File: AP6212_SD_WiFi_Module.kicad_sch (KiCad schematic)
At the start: 21 parts, among them J1 Conn_Coaxial, J2 TF_Card, U1 AP6212, X1 32.768KHz, Y1 26MHz

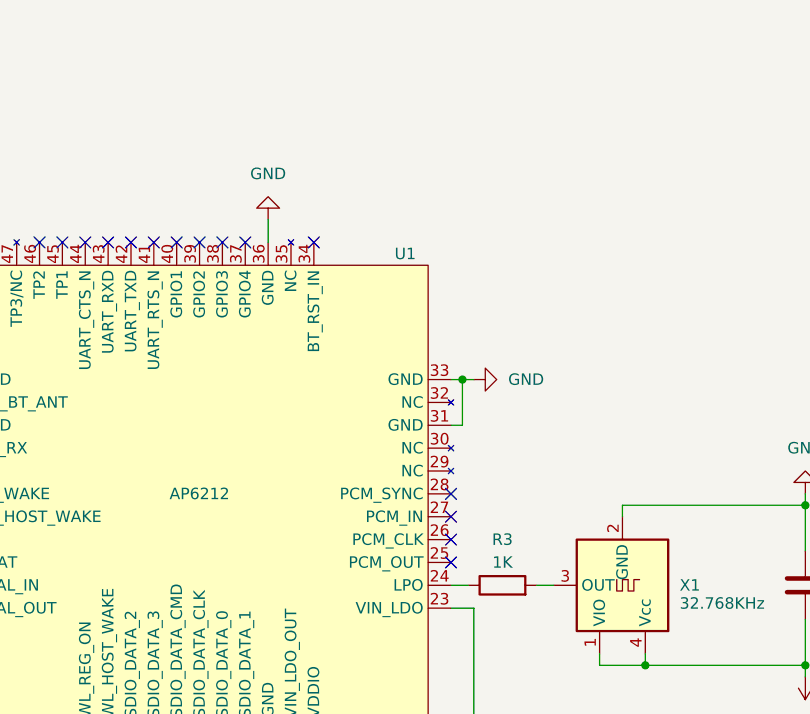
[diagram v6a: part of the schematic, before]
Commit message: BT_RST_N must be driven high or low(not left floating)
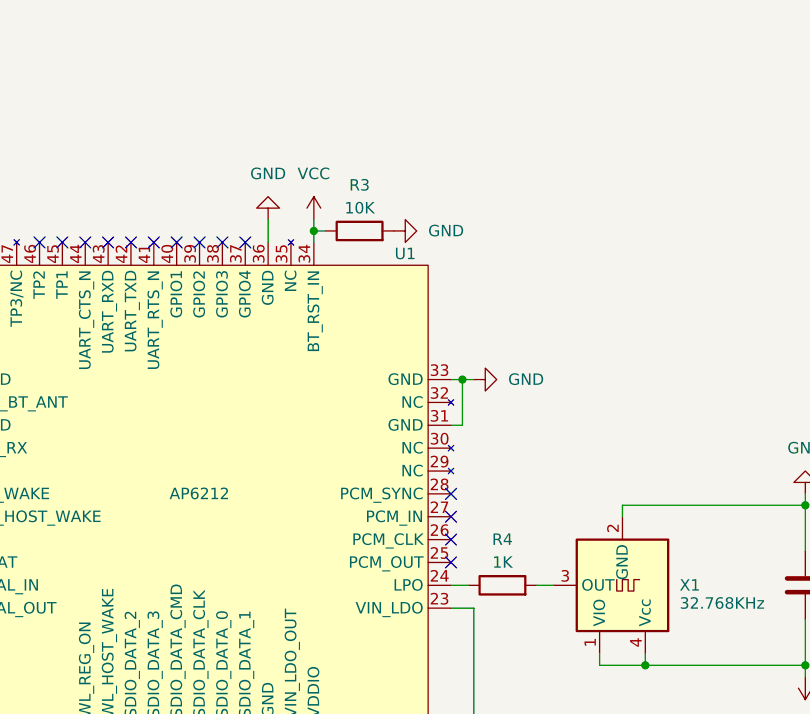
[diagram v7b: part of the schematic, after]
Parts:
- added R3: 10K, Resistor_SMD:R_0603_1608Metric, symbol Device:R
- renumbered R3 to R4
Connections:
- net GND: now also R3.2
- net VCC: now also U1.34 (BT_RST_IN), R3.1
- no-connect marks 19 -> 18
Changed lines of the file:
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@@
   (junction (at 222.25 156.21) (diameter 0) (color 0 0 0 0)
+  )
+  (junction (at 185.42 107.95) (diameter 0) (color 0 0 0 0)
   )
   (junction (at 110.49 147.32) (diameter 0) (color 0 0 0 0)
@@
   (no_connect (at 144.78 137.16))
   (no_connect (at 165.1 109.22))
-  (no_connect (at 185.42 109.22))
   (no_connect (at 200.66 144.78))
   (no_connect (at 170.18 109.22))
@@
     (stroke (width 0) (type default))
   )
+  (wire (pts (xy 185.42 107.95) (xy 185.42 109.22))
+    (stroke (width 0) (type default))
+  )
   (wire (pts (xy 120.65 97.79) (xy 120.65 110.49))
     (stroke (width 0) (type default))
@@
     (stroke (width 0) (type default))
   )
+  (wire (pts (xy 185.42 106.68) (xy 185.42 107.95))
+    (stroke (width 0) (type default))
+  )
   (wire (pts (xy 200.66 129.54) (xy 201.93 129.54))
     (stroke (width 0) (type default))
@@
   )
   (wire (pts (xy 180.34 106.68) (xy 180.34 109.22))
+    (stroke (width 0) (type default))
+  )
+  (wire (pts (xy 185.42 107.95) (xy 186.69 107.95))
     (stroke (width 0) (type default))
   )
@@
   (symbol (lib_id "power:GND") (at 203.2 124.46 90) (unit 1)
     (in_bom yes) (on_board yes) (dnp no) (fields_autoplaced)
-    (property "Reference" "#PWR016" (at 209.55 124.46 0)
+    (property "Reference" "#PWR018" (at 209.55 124.46 0)
       (effects (font (size 1.27 1.27)) hide)
     )
@@
       (project "AP6212_SD_WiFi_Module"
         (path "/b65838ac-496f-4a8d-9112-1df66a66b3df"
-          (reference "#PWR016") (unit 1)
+          (reference "#PWR018") (unit 1)
         )
       )
@@
   (symbol (lib_id "power:VCC") (at 240.03 157.48 180) (unit 1)
     (in_bom yes) (on_board yes) (dnp no) (fields_autoplaced)
-    (property "Reference" "#PWR020" (at 240.03 153.67 0)
+    (property "Reference" "#PWR022" (at 240.03 153.67 0)
       (effects (font (size 1.27 1.27)) hide)
     )
@@
       (project "AP6212_SD_WiFi_Module"
         (path "/b65838ac-496f-4a8d-9112-1df66a66b3df"
-          (reference "#PWR020") (unit 1)
+          (reference "#PWR022") (unit 1)
         )
       )
@@
     )
   )
+  (symbol (lib_id "power:GND") (at 194.31 107.95 90) (unit 1)
+    (in_bom yes) (on_board yes) (dnp no) (fields_autoplaced)
+    (property "Reference" "#PWR017" (at 200.66 107.95 0)
+      (effects (font (size 1.27 1.27)) hide)
+    )
+    (property "Value" "GND" (at 198.12 107.95 90)
+      (effects (font (size 1.27 1.27)) (justify right))
+    )
+    (property "Footprint" "" (at 194.31 107.95 0)
+      (effects (font (size 1.27 1.27)) hide)
+    )
+    (property "Datasheet" "" (at 194.31 107.95 0)
+      (effects (font (size 1.27 1.27)) hide)
+    )
+    (pin "1")
+    (instances
+      (project "AP6212_SD_WiFi_Module"
+        (path "/b65838ac-496f-4a8d-9112-1df66a66b3df"
+          (reference "#PWR017") (unit 1)
+        )
+      )
+    )
+  )
   (symbol (lib_id "Device:C_Small") (at 115.57 110.49 90) (unit 1)
     (in_bom yes) (on_board yes) (dnp no) (fields_autoplaced)
@@
     )
   )
+  (symbol (lib_id "power:VCC") (at 185.42 106.68 0) (unit 1)
+    (in_bom yes) (on_board yes) (dnp no) (fields_autoplaced)
+    (property "Reference" "#PWR014" (at 185.42 110.49 0)
+      (effects (font (size 1.27 1.27)) hide)
+    )
+    (property "Value" "VCC" (at 185.42 101.6 0)
+      (effects (font (size 1.27 1.27)))
+    )
+    (property "Footprint" "" (at 185.42 106.68 0)
+      (effects (font (size 1.27 1.27)) hide)
+    )
+    (property "Datasheet" "" (at 185.42 106.68 0)
+      (effects (font (size 1.27 1.27)) hide)
+    )
+    (pin "1")
+    (instances
+      (project "AP6212_SD_WiFi_Module"
+        (path "/b65838ac-496f-4a8d-9112-1df66a66b3df"
+          (reference "#PWR014") (unit 1)
+        )
+      )
+    )
+  )
   (symbol (lib_id "power:VCC") (at 262.89 134.62 90) (mirror x) (unit 1)
     (in_bom yes) (on_board yes) (dnp no) (fields_autoplaced)
-    (property "Reference" "#PWR022" (at 266.7 134.62 0)
+    (property "Reference" "#PWR024" (at 266.7 134.62 0)
       (effects (font (size 1.27 1.27)) hide)
     )
@@
       (project "AP6212_SD_WiFi_Module"
         (path "/b65838ac-496f-4a8d-9112-1df66a66b3df"
-          (reference "#PWR022") (unit 1)
+          (reference "#PWR024") (unit 1)
         )
       )
@@
   (symbol (lib_id "power:VCC") (at 186.69 166.37 270) (unit 1)
     (in_bom yes) (on_board yes) (dnp no) (fields_autoplaced)
-    (property "Reference" "#PWR015" (at 182.88 166.37 0)
+    (property "Reference" "#PWR016" (at 182.88 166.37 0)
       (effects (font (size 1.27 1.27)) hide)
     )
@@
       (project "AP6212_SD_WiFi_Module"
         (path "/b65838ac-496f-4a8d-9112-1df66a66b3df"
+          (reference "#PWR016") (unit 1)
+        )
+      )
+    )
+  )
+  (symbol (lib_id "power:GND") (at 185.42 177.8 0) (unit 1)
+    (in_bom yes) (on_board yes) (dnp no) (fields_autoplaced)
+    (property "Reference" "#PWR015" (at 185.42 184.15 0)
+      (effects (font (size 1.27 1.27)) hide)
+    )
+    (property "Value" "GND" (at 185.42 182.88 0)
+      (effects (font (size 1.27 1.27)))
+    )
+    (property "Footprint" "" (at 185.42 177.8 0)
+      (effects (font (size 1.27 1.27)) hide)
+    )
+    (property "Datasheet" "" (at 185.42 177.8 0)
+      (effects (font (size 1.27 1.27)) hide)
+    )
+    (pin "1")
+    (instances
+      (project "AP6212_SD_WiFi_Module"
+        (path "/b65838ac-496f-4a8d-9112-1df66a66b3df"
           (reference "#PWR015") (unit 1)
-        )
-      )
-    )
-  )
-  (symbol (lib_id "power:GND") (at 185.42 177.8 0) (unit 1)
-    (in_bom yes) (on_board yes) (dnp no) (fields_autoplaced)
-    (property "Reference" "#PWR014" (at 185.42 184.15 0)
-      (effects (font (size 1.27 1.27)) hide)
-    )
-    (property "Value" "GND" (at 185.42 182.88 0)
-      (effects (font (size 1.27 1.27)))
-    )
-    (property "Footprint" "" (at 185.42 177.8 0)
-      (effects (font (size 1.27 1.27)) hide)
-    )
-    (property "Datasheet" "" (at 185.42 177.8 0)
-      (effects (font (size 1.27 1.27)) hide)
-    )
-    (pin "1")
-    (instances
-      (project "AP6212_SD_WiFi_Module"
-        (path "/b65838ac-496f-4a8d-9112-1df66a66b3df"
-          (reference "#PWR014") (unit 1)
         )
       )
@@
   (symbol (lib_id "power:GND") (at 240.03 137.16 180) (unit 1)
     (in_bom yes) (on_board yes) (dnp no) (fields_autoplaced)
-    (property "Reference" "#PWR019" (at 240.03 130.81 0)
+    (property "Reference" "#PWR021" (at 240.03 130.81 0)
       (effects (font (size 1.27 1.27)) hide)
     )
@@
       (project "AP6212_SD_WiFi_Module"
         (path "/b65838ac-496f-4a8d-9112-1df66a66b3df"
-          (reference "#PWR019") (unit 1)
+          (reference "#PWR021") (unit 1)
         )
       )
@@
   (symbol (lib_id "Device:R") (at 206.375 147.32 90) (unit 1)
     (in_bom yes) (on_board yes) (dnp no)
-    (property "Reference" "R3" (at 206.375 142.24 90)
+    (property "Reference" "R4" (at 206.375 142.24 90)
       (effects (font (size 1.27 1.27)))
     )
@@
       (project "AP6212_SD_WiFi_Module"
         (path "/b65838ac-496f-4a8d-9112-1df66a66b3df"
-          (reference "R3") (unit 1)
+          (reference "R4") (unit 1)
         )
       )
@@
   (symbol (lib_id "power:VCC") (at 213.36 60.96 180) (unit 1)
     (in_bom yes) (on_board yes) (dnp no) (fields_autoplaced)
-    (property "Reference" "#PWR017" (at 213.36 57.15 0)
+    (property "Reference" "#PWR019" (at 213.36 57.15 0)
       (effects (font (size 1.27 1.27)) hide)
     )
@@
       (project "AP6212_SD_WiFi_Module"
         (path "/b65838ac-496f-4a8d-9112-1df66a66b3df"
-          (reference "#PWR017") (unit 1)
+          (reference "#PWR019") (unit 1)
         )
       )
@@
   (symbol (lib_id "power:GND") (at 228.6 60.96 0) (unit 1)
     (in_bom yes) (on_board yes) (dnp no) (fields_autoplaced)
-    (property "Reference" "#PWR018" (at 228.6 67.31 0)
+    (property "Reference" "#PWR020" (at 228.6 67.31 0)
       (effects (font (size 1.27 1.27)) hide)
     )
@@
       (project "AP6212_SD_WiFi_Module"
         (path "/b65838ac-496f-4a8d-9112-1df66a66b3df"
-          (reference "#PWR018") (unit 1)
+          (reference "#PWR020") (unit 1)
         )
       )
@@
   (symbol (lib_id "power:GND") (at 262.89 129.54 270) (mirror x) (unit 1)
     (in_bom yes) (on_board yes) (dnp no) (fields_autoplaced)
-    (property "Reference" "#PWR021" (at 256.54 129.54 0)
+    (property "Reference" "#PWR023" (at 256.54 129.54 0)
       (effects (font (size 1.27 1.27)) hide)
     )
@@
       (project "AP6212_SD_WiFi_Module"
         (path "/b65838ac-496f-4a8d-9112-1df66a66b3df"
-          (reference "#PWR021") (unit 1)
-        )
-      )
+          (reference "#PWR023") (unit 1)
+        )
+      )
+    )
+  )
+  (symbol (lib_id "Device:R") (at 190.5 107.95 90) (unit 1)
+    (in_bom yes) (on_board yes) (dnp no)
+    (property "Reference" "R3" (at 190.5 102.87 90)
+      (effects (font (size 1.27 1.27)))
+    )
+    (property "Value" "10K" (at 190.5 105.41 90)
+      (effects (font (size 1.27 1.27)))
+    )
+    (property "Footprint" "Resistor_SMD:R_0603_1608Metric" (at 190.5 109.728 90)
+      (effects (font (size 1.27 1.27)) hide)
+    )
+    (property "Datasheet" "~" (at 190.5 107.95 0)
+      (effects (font (size 1.27 1.27)) hide)
+    )
+    (pin "1")
+    (pin "2")
+    (instances
+      (project "AP6212_SD_WiFi_Module"
+        (path "/b65838ac-496f-4a8d-9112-1df66a66b3df"
+          (reference "R3") (unit 1)
+        )
+      )
